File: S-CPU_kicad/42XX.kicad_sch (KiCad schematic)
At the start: 161 parts, among them U34 OR_2, U35 OR_2, U36 OR_2, U37 OR_2, U6 MUX

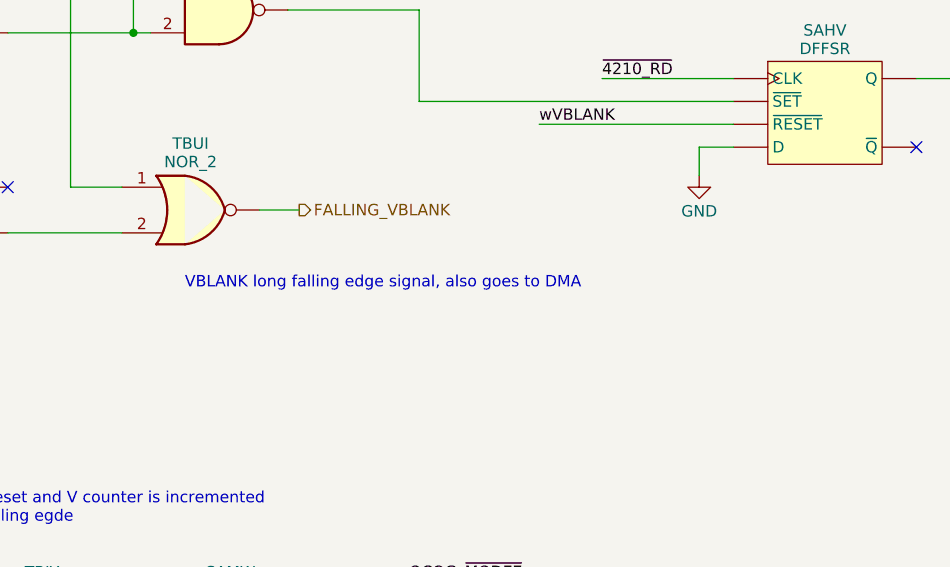
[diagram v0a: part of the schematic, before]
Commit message: Progress in DMA section. Fixed some DFF output issues.
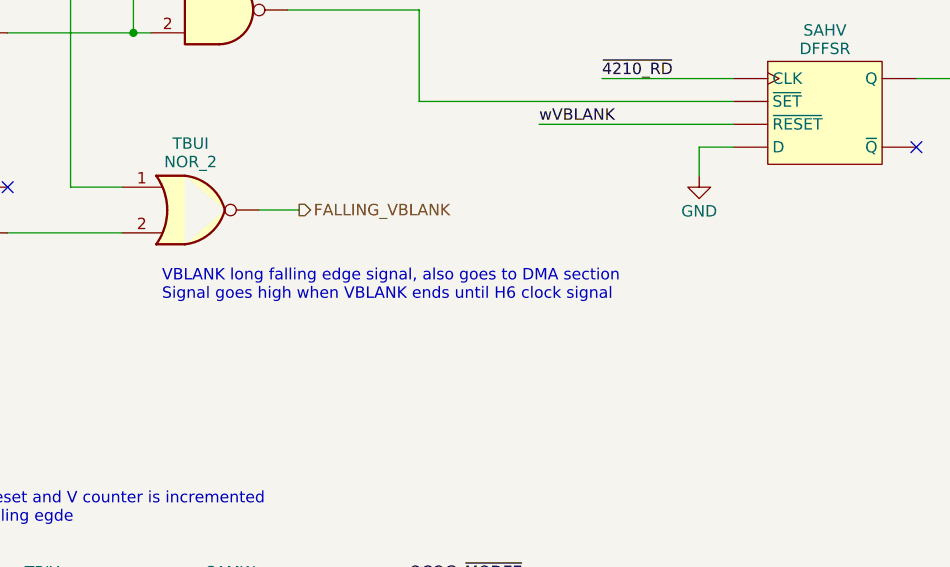
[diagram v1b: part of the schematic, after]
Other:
- note added: "VBLANK long falling edge signal, also goes to DMA section Signal goes high when VBLANK ends until H6 clock signal"
- note removed: "VBLANK long falling edge signal, also goes to DMA"
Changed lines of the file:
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@@
     (effects (font (size 5 5) (thickness 1) bold) (justify left bottom))
   )
-  (text "VBLANK long falling edge signal, also goes to DMA" (at 345.44 182.88 0)
+  (text "VBLANK long falling edge signal, also goes to DMA section\nSignal goes high when VBLANK ends until H6 clock signal"
+    (at 342.9 184.15 0)
     (effects (font (size 1.27 1.27)) (justify left bottom))
   )

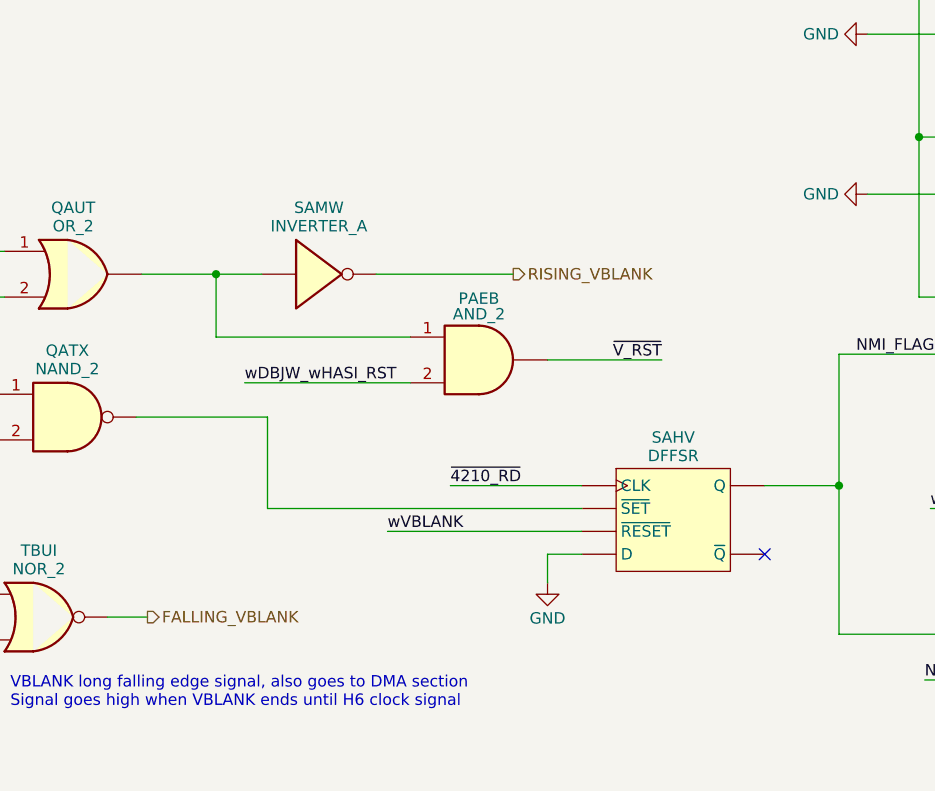
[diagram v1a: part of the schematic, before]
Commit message: Update in DMA sections - most debug signals identified. Error found in SYS clk generation. Simulation show correct 6, 8 and 12 cycle SYSCLK modes.
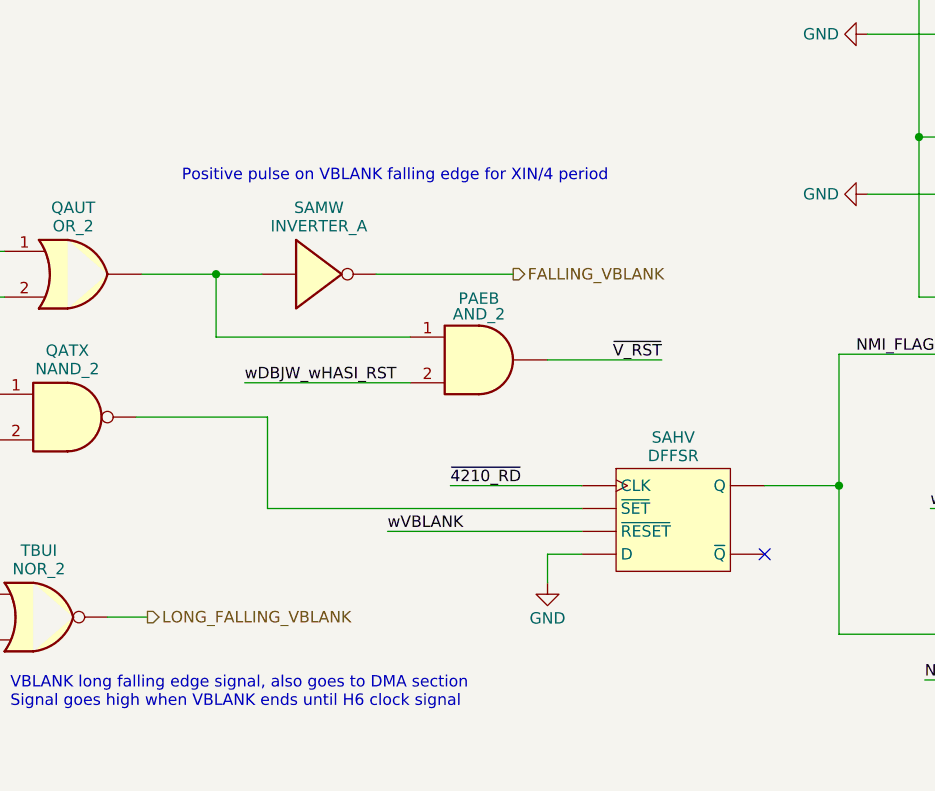
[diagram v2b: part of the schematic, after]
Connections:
- net RISING_VBLANK is gone; now on net FALLING_VBLANK: SAMW.2
- net FALLING_VBLANK: no longer TBUI.3
- new net LONG_FALLING_VBLANK: TBUI.3
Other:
- note added: "Positive pulse on VBLANK falling edge for XIN/4 period"
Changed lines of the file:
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@@
     (effects (font (size 5 5) (thickness 1) bold) (justify left bottom))
+  )
+  (text "Positive pulse on VBLANK falling edge for XIN/4 period"
+    (at 361.95 125.73 0)
+    (effects (font (size 1.27 1.27)) (justify left bottom))
   )
   (text "CPU version 2\nD3-0 = \"0010\"" (at 480.695 97.79 0)
@@
     (effects (font (size 1.27 1.27)) (justify left))
   )
-  (hierarchical_label "RISING_VBLANK" (shape output) (at 398.78 135.89 0) (fields_autoplaced)
+  (hierarchical_label "FALLING_VBLANK" (shape output) (at 398.78 135.89 0) (fields_autoplaced)
     (effects (font (size 1.27 1.27)) (justify left))
   )
@@
     (effects (font (size 1.27 1.27)) (justify right))
   )
-  (hierarchical_label "FALLING_VBLANK" (shape output) (at 358.14 173.99 0) (fields_autoplaced)
-    (effects (font (size 1.27 1.27)) (justify left))
-  )
+  (hierarchical_label "LONG_FALLING_VBLANK" (shape output) (at 358.14 173.99 0) (fields_autoplaced)
+    (effects (font (size 1.27 1.27)) (justify left))
+  )

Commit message: Schematics update.
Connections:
- net wNBRL_wNBQA_XIN/4 renamed wNBRL_wNBQA_~{XIN/4}
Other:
- note removed: "4200 WRITE"
- company: Regis Galland -> Author: Regis Galland
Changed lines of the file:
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@@
     (date "2023-06-14")
     (rev "0.1")
-    (company "Regis Galland")
+    (company "Author: Regis Galland")
   )
   (junction (at 125.095 448.31) (diameter 0) (color 0 0 0 0)
@@
     (effects (font (size 5 5) (thickness 1) bold) (justify left bottom))
   )
-  (text "4200 WRITE" (at 309.88 292.1 0)
-    (effects (font (size 5 5) (thickness 1) bold) (justify left bottom))
-  )
   (text "4210 READ" (at 439.42 63.5 0)
     (effects (font (size 5 5) (thickness 1) bold) (justify left bottom))
@@
     (effects (font (size 1.27 1.27)) (justify left bottom))
   )
-  (label "wNBRL_wNBQA_XIN{slash}4" (at 535.305 229.87 0) (fields_autoplaced)
+  (label "wNBRL_wNBQA_~{XIN{slash}4}" (at 535.305 229.87 0) (fields_autoplaced)
     (effects (font (size 1.27 1.27)) (justify left bottom))
   )
@@
     (effects (font (size 1.27 1.27)) (justify right bottom))
   )
-  (label "wNBRL_wNBQA_XIN{slash}4" (at 363.22 226.695 0) (fields_autoplaced)
+  (label "wNBRL_wNBQA_~{XIN{slash}4}" (at 363.22 226.695 0) (fields_autoplaced)
     (effects (font (size 1.27 1.27)) (justify left bottom))
   )
@@
     (effects (font (size 1.27 1.27)) (justify right bottom))
   )
-  (label "wNBRL_wNBQA_XIN{slash}4" (at 273.685 133.35 0) (fields_autoplaced)
+  (label "wNBRL_wNBQA_~{XIN{slash}4}" (at 273.685 133.35 0) (fields_autoplaced)
     (effects (font (size 1.27 1.27)) (justify left bottom))
   )
@@
     (effects (font (size 1.27 1.27)) (justify left bottom))
   )
-  (label "wNBRL_wNBQA_XIN{slash}4" (at 257.81 219.075 0) (fields_autoplaced)
+  (label "wNBRL_wNBQA_~{XIN{slash}4}" (at 257.81 219.075 0) (fields_autoplaced)
     (effects (font (size 1.27 1.27)) (justify left bottom))
   )
@@
     (effects (font (size 1.27 1.27)) (justify left bottom))
   )
-  (label "wNBRL_wNBQA_XIN{slash}4" (at 554.99 115.57 0) (fields_autoplaced)
+  (label "wNBRL_wNBQA_~{XIN{slash}4}" (at 554.99 115.57 0) (fields_autoplaced)
     (effects (font (size 1.27 1.27)) (justify left bottom))
   )
@@
     (effects (font (size 1.27 1.27)) (justify left))
   )
-  (hierarchical_label "wNBRL_wNBQA_XIN{slash}4" (shape input) (at 273.685 133.35 180) (fields_autoplaced)
+  (hierarchical_label "wNBRL_wNBQA_~{XIN{slash}4}" (shape input) (at 273.685 133.35 180) (fields_autoplaced)
     (effects (font (size 1.27 1.27)) (justify right))
   )
